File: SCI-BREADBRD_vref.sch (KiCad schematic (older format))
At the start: 17 parts, among them P10 TP, P11 TP, P12 CONN_1X2, U8 OPA454AIDDA, U9 OPA454AIDDA

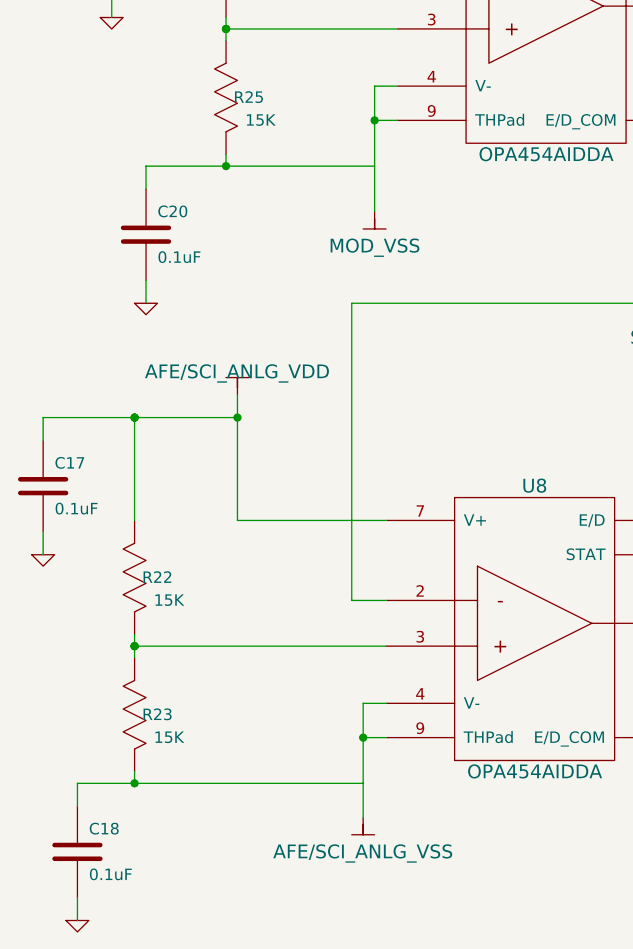
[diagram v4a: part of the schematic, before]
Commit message: Added some bypass caps. Rearranged pins on connectors to make layout easier.
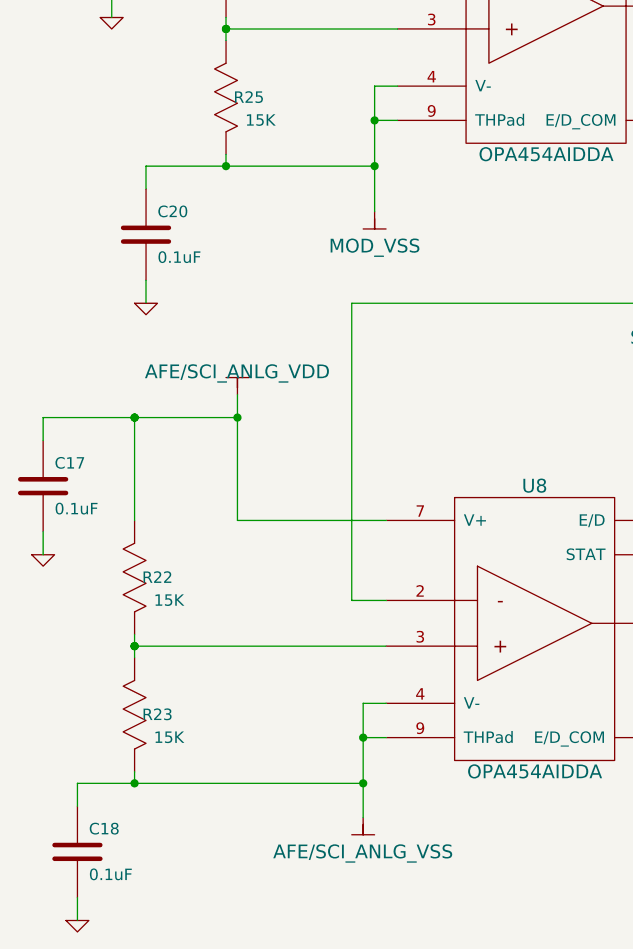
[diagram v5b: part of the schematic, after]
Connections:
- wire segments 64 -> 62
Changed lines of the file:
@@
-EESchema Schematic File Version 2  date Wed 02 May 2012 02:37:03 AM EDT
+EESchema Schematic File Version 2  date Wed 02 May 2012 11:11:08 PM EDT
 LIBS:custom_transistors
 LIBS:TI_custom
@@
 Sheet 9 9
 Title "SCI-BREADBRD-MVK"
-Date "2 may 2012"
+Date "3 may 2012"
 Rev "A"
 Comp "The Ohio State University"
@@
 $EndComp
 $Comp
-L GND #PWR083
+L GND #PWR082
 U 1 1 4F8FA231
 P 6400 5950
-F 0 "#PWR083" H 6400 5950 30  0001 C CNN
+F 0 "#PWR082" H 6400 5950 30  0001 C CNN
 F 1 "GND" H 6400 5880 30  0001 C CNN
 	1    6400 5950
@@
 $EndComp
 $Comp
-L GND #PWR084
+L GND #PWR083
 U 1 1 4F8FA8AC
 P 6450 3250
-F 0 "#PWR084" H 6450 3250 30  0001 C CNN
+F 0 "#PWR083" H 6450 3250 30  0001 C CNN
 F 1 "GND" H 6450 3180 30  0001 C CNN
 	1    6450 3250
@@
 $EndComp
 $Comp
-L GND #PWR085
+L GND #PWR084
 U 1 1 4F8F7B5C
 P 3800 2700
-F 0 "#PWR085" H 3800 2700 30  0001 C CNN
+F 0 "#PWR084" H 3800 2700 30  0001 C CNN
 F 1 "GND" H 3800 2630 30  0001 C CNN
 	1    3800 2700
@@
 $EndComp
 $Comp
-L GND #PWR086
+L GND #PWR085
 U 1 1 4F8F8028
 P 3500 5050
-F 0 "#PWR086" H 3500 5050 30  0001 C CNN
+F 0 "#PWR085" H 3500 5050 30  0001 C CNN
 F 1 "GND" H 3500 4980 30  0001 C CNN
 	1    3500 5050
@@
 $EndComp
 $Comp
-L GND #PWR087
+L GND #PWR086
 U 1 1 4F8F839D
 P 3950 3950
-F 0 "#PWR087" H 3950 3950 30  0001 C CNN
+F 0 "#PWR086" H 3950 3950 30  0001 C CNN
 F 1 "GND" H 3950 3880 30  0001 C CNN
 	1    3950 3950
@@
 $EndComp
 $Comp
-L GND #PWR088
+L GND #PWR087
 U 1 1 4F8F8442
 P 3650 6650
-F 0 "#PWR088" H 3650 6650 30  0001 C CNN
+F 0 "#PWR087" H 3650 6650 30  0001 C CNN
 F 1 "GND" H 3650 6580 30  0001 C CNN
 	1    3650 6650
@@
 	1    0    0    -1
 $EndComp
-Wire Wire Line
-	4900 6050 3650 6050
-Wire Wire Line
-	4350 4350 4350 4900
-Wire Wire Line
-	4350 4900 5000 4900
-Wire Wire Line
-	3900 6050 3900 6000
-Wire Wire Line
-	3900 4900 3900 4450
-Connection ~ 4350 4450
-Wire Wire Line
-	3900 5400 3900 5500
-Wire Wire Line
-	3900 5450 5000 5450
-Connection ~ 3900 5450
-Connection ~ 3900 5450
-Wire Wire Line
-	4400 6050 4400 6050
-Wire Wire Line
-	5000 5700 4900 5700
-Wire Wire Line
-	4900 5700 4900 6200
-Wire Wire Line
-	5000 5850 4900 5850
-Connection ~ 4900 5850
-Wire Wire Line
-	5000 5250 4850 5250
-Wire Wire Line
-	4850 5250 4850 3950
-Wire Wire Line
-	4850 3950 7450 3950
-Wire Wire Line
-	7450 3300 7450 5350
-Wire Wire Line
-	6300 5850 6400 5850
-Wire Wire Line
-	6400 5850 6400 5950
-Wire Wire Line
-	7200 5050 7200 4950
-Wire Wire Line
-	6400 4250 6400 4350
-Wire Wire Line
-	6400 4850 6400 4900
-Wire Wire Line
-	6400 4900 6300 4900
-Wire Wire Line
-	4950 3350 3950 3350
-Wire Wire Line
-	4500 1650 4500 2200
-Wire Wire Line
-	4500 2200 5050 2200
-Wire Wire Line
-	4300 3350 4300 3300
-Wire Wire Line
-	4300 2200 4300 2100
-Wire Wire Line
-	4300 2700 4300 2800
-Wire Wire Line
-	4300 2750 5050 2750
-Connection ~ 4300 2750
-Connection ~ 4300 2750
-Wire Wire Line
-	4550 3350 4550 3350
-Wire Wire Line
-	5050 3000 4950 3000
-Wire Wire Line
-	4950 3000 4950 3550
-Wire Wire Line
-	5050 3150 4950 3150
-Connection ~ 4950 3150
-Wire Wire Line
-	5050 2550 4900 2550
-Wire Wire Line
-	4900 2550 4900 1250
-Wire Wire Line
-	4900 1250 7500 1250
-Wire Wire Line
-	7500 1250 7500 3100
-Wire Wire Line
-	6350 3150 6450 3150
-Wire Wire Line
-	6450 3150 6450 3250
-Wire Wire Line
-	7200 2350 7200 2250
-Wire Wire Line
-	6450 1550 6450 1650
-Wire Wire Line
-	6450 2150 6450 2200
-Wire Wire Line
-	6450 2200 6350 2200
-Wire Wire Line
-	7450 5350 6300 5350
-Wire Wire Line
-	7500 2650 6350 2650
-Wire Wire Line
-	7500 3100 7800 3100
-Connection ~ 7500 2650
-Wire Wire Line
-	7450 3300 7800 3300
-Connection ~ 7450 3950
-Wire Wire Line
-	3800 2700 3800 2600
-Wire Wire Line
-	3800 2200 3800 2100
-Wire Wire Line
-	3800 2100 4500 2100
-Connection ~ 4500 2100
-Connection ~ 4300 2100
-Wire Wire Line
-	3500 5050 3500 4950
-Wire Wire Line
-	3500 4550 3500 4450
-Wire Wire Line
-	3500 4450 4350 4450
-Connection ~ 3900 4450
-Connection ~ 3900 4450
-Wire Wire Line
-	3950 3950 3950 3850
-Wire Wire Line
-	3950 3350 3950 3450
-Connection ~ 4300 3350
-Wire Wire Line
-	3650 6650 3650 6550
-Wire Wire Line
-	3650 6050 3650 6150
-Connection ~ 3900 6050
-Wire Wire Line
-	6750 4450 6750 4300
-Connection ~ 6450 1600
-Wire Wire Line
-	6300 5050 7200 5050
-Wire Wire Line
-	6750 4950 6750 5050
-Connection ~ 6750 5050
-Wire Wire Line
-	6350 2350 7200 2350
-Wire Wire Line
-	6750 2350 6750 2300
-Connection ~ 6750 2350
-Wire Wire Line
-	6450 1600 6750 1600
-Wire Wire Line
-	6750 1600 6750 1800
-Wire Wire Line
-	6750 4300 6400 4300
-Connection ~ 6400 4300
 $Comp
 L TP P10
@@
 $EndComp
 $Comp
-L MOD_VDD #PWR089
+L MOD_VDD #PWR088
 U 1 1 4F9AECA0
 P 4500 1650
-F 0 "#PWR089" H 4500 1750 30  0001 C CNN
+F 0 "#PWR088" H 4500 1750 30  0001 C CNN
 F 1 "MOD_VDD" H 4500 1800 60  0000 C CNN
 	1    4500 1650
@@
 $EndComp
 $Comp
-L MOD_VSS #PWR090
+L MOD_VSS #PWR089
 U 1 1 4F9AECAF
 P 4950 3550
-F 0 "#PWR090" H 4950 3450 30  0001 C CNN
+F 0 "#PWR089" H 4950 3450 30  0001 C CNN
 F 1 "MOD_VSS" H 4950 3400 60  0000 C CNN
 	1    4950 3550
@@
 $EndComp
 $Comp
-L SCI_DVDD_3_3V #PWR091
+L SCI_DVDD_3_3V #PWR090
 U 1 1 4F9AECC8
 P 6450 1550
-F 0 "#PWR091" H 6450 1650 30  0001 C CNN
+F 0 "#PWR090" H 6450 1650 30  0001 C CNN
 F 1 "SCI_DVDD_3_3V" H 6450 1700 60  0000 C CNN
 	1    6450 1550
@@
 $EndComp
 $Comp
-L SCI_DVDD_3_3V #PWR092
+L SCI_DVDD_3_3V #PWR091
 U 1 1 4F9AECD7
 P 6400 4250
-F 0 "#PWR092" H 6400 4350 30  0001 C CNN
+F 0 "#PWR091" H 6400 4350 30  0001 C CNN
 F 1 "SCI_DVDD_3_3V" H 6400 4400 60  0000 C CNN
 	1    6400 4250
@@
 $EndComp
 $Comp
-L AFE/SCI_ANLG_VDD #PWR093
+L AFE/SCI_ANLG_VDD #PWR092
 U 1 1 4F9AECE6
 P 4350 4350
-F 0 "#PWR093" H 4350 4450 30  0001 C CNN
+F 0 "#PWR092" H 4350 4450 30  0001 C CNN
 F 1 "AFE/SCI_ANLG_VDD" H 4350 4450 60  0000 C CNN
 	1    4350 4350
@@
 $EndComp
 $Comp
-L AFE/SCI_ANLG_VSS #PWR094
+L AFE/SCI_ANLG_VSS #PWR093
 U 1 1 4F9AECF5
 P 4900 6200
-F 0 "#PWR094" H 4900 6100 30  0001 C CNN
+F 0 "#PWR093" H 4900 6100 30  0001 C CNN
 F 1 "AFE/SCI_ANLG_VSS" H 4900 6050 60  0000 C CNN
 	1    4900 6200
 	1    0    0    -1
 $EndComp
+Wire Wire Line
+	4350 4350 4350 4900
+Wire Wire Line
+	4350 4900 5000 4900
+Wire Wire Line
+	3900 6050 3900 6000
+Wire Wire Line
+	3900 4900 3900 4450
+Connection ~ 4350 4450
+Wire Wire Line
+	3900 5400 3900 5500
+Wire Wire Line
+	3900 5450 5000 5450
+Connection ~ 3900 5450
+Connection ~ 3900 5450
+Wire Wire Line
+	5000 5700 4900 5700
+Wire Wire Line
+	4900 5700 4900 6200
+Wire Wire Line
+	5000 5850 4900 5850
+Connection ~ 4900 5850
+Wire Wire Line
+	5000 5250 4850 5250
+Wire Wire Line
+	4850 5250 4850 3950
+Wire Wire Line
+	4850 3950 7450 3950
+Wire Wire Line
+	7450 3300 7450 5350
+Wire Wire Line
+	6300 5850 6400 5850
+Wire Wire Line
+	6400 5850 6400 5950
+Wire Wire Line
+	7200 5050 7200 4950
+Wire Wire Line
+	6400 4250 6400 4350
+Wire Wire Line
+	6400 4850 6400 4900
+Wire Wire Line
+	6400 4900 6300 4900
+Wire Wire Line
+	4500 1650 4500 2200
+Wire Wire Line
+	4500 2200 5050 2200
+Wire Wire Line
+	4300 3350 4300 3300
+Wire Wire Line
+	4300 2200 4300 2100
+Wire Wire Line
+	4300 2700 4300 2800
+Wire Wire Line
+	4300 2750 5050 2750
+Connection ~ 4300 2750
+Connection ~ 4300 2750
+Wire Wire Line
+	5050 3000 4950 3000
+Wire Wire Line
+	4950 3000 4950 3550
+Wire Wire Line
+	5050 3150 4950 3150
+Connection ~ 4950 3150
+Wire Wire Line
+	5050 2550 4900 2550
+Wire Wire Line
+	4900 2550 4900 1250
+Wire Wire Line
+	4900 1250 7500 1250
+Wire Wire Line
+	7500 1250 7500 3100
+Wire Wire Line
+	6350 3150 6450 3150
+Wire Wire Line
+	6450 3150 6450 3250
+Wire Wire Line
+	7200 2350 7200 2250
+Wire Wire Line
+	6450 1550 6450 1650
+Wire Wire Line
+	6450 2150 6450 2200
+Wire Wire Line
+	6450 2200 6350 2200
+Wire Wire Line
+	7450 5350 6300 5350
+Wire Wire Line
+	7500 2650 6350 2650
+Wire Wire Line
+	7500 3100 7800 3100
+Connection ~ 7500 2650
+Wire Wire Line
+	7450 3300 7800 3300
+Connection ~ 7450 3950
+Wire Wire Line
+	3800 2700 3800 2600
+Wire Wire Line
+	3800 2200 3800 2100
+Wire Wire Line
+	3800 2100 4500 2100
+Connection ~ 4500 2100
+Connection ~ 4300 2100
+Wire Wire Line
+	3500 5050 3500 4950
+Wire Wire Line
+	3500 4550 3500 4450
+Wire Wire Line
+	3500 4450 4350 4450
+Connection ~ 3900 4450
+Connection ~ 3900 4450
+Wire Wire Line
+	3950 3950 3950 3850
+Wire Wire Line
+	3950 3350 3950 3450
+Connection ~ 4300 3350
+Wire Wire Line
+	3650 6650 3650 6550
+Wire Wire Line
+	3650 6050 3650 6150
+Connection ~ 3900 6050
+Wire Wire Line
+	6750 4450 6750 4300
+Connection ~ 6450 1600
+Wire Wire Line
+	6300 5050 7200 5050
+Wire Wire Line
+	6750 4950 6750 5050
+Connection ~ 6750 5050
+Wire Wire Line
+	6350 2350 7200 2350
+Wire Wire Line
+	6750 2350 6750 2300
+Connection ~ 6750 2350
+Wire Wire Line
+	6450 1600 6750 1600
+Wire Wire Line
+	6750 1600 6750 1800
+Wire Wire Line
+	6750 4300 6400 4300
+Connection ~ 6400 4300
+Wire Wire Line
+	3950 3350 4950 3350
+Wire Wire Line
+	3650 6050 4900 6050
+Connection ~ 4900 6050
+Connection ~ 4950 3350
 $EndSCHEMATC

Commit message: Finished initial PCB layout
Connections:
- net labels added: HI_VDD, HI_VSS
- net labels removed: AFE/SCI_ANLG_VDD, AFE/SCI_ANLG_VSS
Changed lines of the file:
@@
-EESchema Schematic File Version 2  date Fri 04 May 2012 05:15:56 PM EDT
+EESchema Schematic File Version 2  date Tue 08 May 2012 11:34:32 AM EDT
 LIBS:custom_transistors
 LIBS:TI_custom
@@
 Sheet 9 9
 Title "SCI-BREADBRD-MVK"
-Date "4 may 2012"
+Date "7 may 2012"
 Rev "A"
 Comp "The Ohio State University"
@@
 $EndComp
 $Comp
-L GND #PWR089
+L GND #PWR097
 U 1 1 4F8FA231
 P 6400 5950
-F 0 "#PWR089" H 6400 5950 30  0001 C CNN
+F 0 "#PWR097" H 6400 5950 30  0001 C CNN
 F 1 "GND" H 6400 5880 30  0001 C CNN
 	1    6400 5950
@@
 $EndComp
 $Comp
-L GND #PWR090
+L GND #PWR098
 U 1 1 4F8FA8AC
 P 6450 3250
-F 0 "#PWR090" H 6450 3250 30  0001 C CNN
+F 0 "#PWR098" H 6450 3250 30  0001 C CNN
 F 1 "GND" H 6450 3180 30  0001 C CNN
 	1    6450 3250
@@
 $EndComp
 $Comp
-L GND #PWR091
+L GND #PWR099
 U 1 1 4F8F7B5C
 P 3800 2700
-F 0 "#PWR091" H 3800 2700 30  0001 C CNN
+F 0 "#PWR099" H 3800 2700 30  0001 C CNN
 F 1 "GND" H 3800 2630 30  0001 C CNN
 	1    3800 2700
@@
 $EndComp
 $Comp
-L GND #PWR092
+L GND #PWR0100
 U 1 1 4F8F8028
 P 3500 5050
-F 0 "#PWR092" H 3500 5050 30  0001 C CNN
+F 0 "#PWR0100" H 3500 5050 30  0001 C CNN
 F 1 "GND" H 3500 4980 30  0001 C CNN
 	1    3500 5050
@@
 $EndComp
 $Comp
-L GND #PWR093
+L GND #PWR0101
 U 1 1 4F8F839D
 P 3950 3950
-F 0 "#PWR093" H 3950 3950 30  0001 C CNN
+F 0 "#PWR0101" H 3950 3950 30  0001 C CNN
 F 1 "GND" H 3950 3880 30  0001 C CNN
 	1    3950 3950
@@
 $EndComp
 $Comp
-L GND #PWR094
+L GND #PWR0102
 U 1 1 4F8F8442
 P 3650 6650
-F 0 "#PWR094" H 3650 6650 30  0001 C CNN
+F 0 "#PWR0102" H 3650 6650 30  0001 C CNN
 F 1 "GND" H 3650 6580 30  0001 C CNN
 	1    3650 6650
@@
 $EndComp
 $Comp
-L MOD_VDD #PWR095
+L MOD_VDD #PWR0103
 U 1 1 4F9AECA0
 P 4500 1650
-F 0 "#PWR095" H 4500 1750 30  0001 C CNN
+F 0 "#PWR0103" H 4500 1750 30  0001 C CNN
 F 1 "MOD_VDD" H 4500 1800 60  0000 C CNN
 	1    4500 1650
@@
 $EndComp
 $Comp
-L MOD_VSS #PWR096
+L MOD_VSS #PWR0104
 U 1 1 4F9AECAF
 P 4950 3550
-F 0 "#PWR096" H 4950 3450 30  0001 C CNN
+F 0 "#PWR0104" H 4950 3450 30  0001 C CNN
 F 1 "MOD_VSS" H 4950 3400 60  0000 C CNN
 	1    4950 3550
@@
 $EndComp
 $Comp
-L SCI_DVDD_3_3V #PWR097
+L SCI_DVDD_3_3V #PWR0105
 U 1 1 4F9AECC8
 P 6450 1550
-F 0 "#PWR097" H 6450 1650 30  0001 C CNN
+F 0 "#PWR0105" H 6450 1650 30  0001 C CNN
 F 1 "SCI_DVDD_3_3V" H 6450 1700 60  0000 C CNN
 	1    6450 1550
@@
 $EndComp
 $Comp
-L SCI_DVDD_3_3V #PWR098
+L SCI_DVDD_3_3V #PWR0106
 U 1 1 4F9AECD7
 P 6400 4250
-F 0 "#PWR098" H 6400 4350 30  0001 C CNN
+F 0 "#PWR0106" H 6400 4350 30  0001 C CNN
 F 1 "SCI_DVDD_3_3V" H 6400 4400 60  0000 C CNN
 	1    6400 4250
-	1    0    0    -1
-$EndComp
-$Comp
-L AFE/SCI_ANLG_VDD #PWR099
-U 1 1 4F9AECE6
-P 4350 4350
-F 0 "#PWR099" H 4350 4450 30  0001 C CNN
-F 1 "AFE/SCI_ANLG_VDD" H 4350 4450 60  0000 C CNN
-	1    4350 4350
-	1    0    0    -1
-$EndComp
-$Comp
-L AFE/SCI_ANLG_VSS #PWR0100
-U 1 1 4F9AECF5
-P 4900 6200
-F 0 "#PWR0100" H 4900 6100 30  0001 C CNN
-F 1 "AFE/SCI_ANLG_VSS" H 4900 6050 60  0000 C CNN
-	1    4900 6200
 	1    0    0    -1
 $EndComp
@@
 Connection ~ 4900 6050
 Connection ~ 4950 3350
+$Comp
+L HI_VDD #PWR0107
+U 1 1 4FA80CBF
+P 4350 4350
+F 0 "#PWR0107" H 4350 4450 30  0001 C CNN
+F 1 "HI_VDD" H 4350 4500 60  0000 C CNN
+	1    4350 4350
+	1    0    0    -1
+$EndComp
+$Comp
+L HI_VSS #PWR0108
+U 1 1 4FA80CCE
+P 4900 6200
+F 0 "#PWR0108" H 4900 6100 30  0001 C CNN
+F 1 "HI_VSS" H 4900 6050 60  0000 C CNN
+	1    4900 6200
+	1    0    0    -1
+$EndComp
 $EndSCHEMATC
